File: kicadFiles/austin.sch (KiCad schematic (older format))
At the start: 469 parts, among them J1 TYPE-C-31-M12_13, J2 Conn_01x04_Male, J5 Conn_01x06_Male, Q1 AO4406AL, SW1 MXSwitch, SW10 MXSwitch, SW100 MXSwitch, SW101 MXSwitch, SW102 MXSwitch, SW103 MXSwitch, SW104 MXSwitch, SW105 MXSwitch, SW106 MXSwitch, SW107 MXSwitch, SW108 MXSwitch, SW109 MXSwitch, SW11 MXSwitch, SW110 MXSwitch, SW111 MXSwitch, SW112 MXSwitch, SW12 MXSwitch, SW13 MXSwitch, SW14 MXSwitch, SW15 MXSwitch, SW16 MXSwitch, SW17 MXSwitch, SW18 MXSwitch, SW19 MXSwitch, SW2 MXSwitch, SW20 MXSwitch, SW21 MXSwitch, SW22 MXSwitch, SW23 MXSwitch, SW24 MXSwitch, SW25 MXSwitch, SW26 MXSwitch, SW27 MXSwitch, SW28 MXSwitch, SW29 MXSwitch, SW3 MXSwitch, SW30 MXSwitch, SW31 MXSwitch, SW32 MXSwitch, SW33 MXSwitch, SW34 MXSwitch, SW35 MXSwitch, SW36 MXSwitch, SW37 MXSwitch, SW38 MXSwitch, SW39 MXSwitch, SW4 MXSwitch, SW40 MXSwitch, SW41 MXSwitch, SW42 MXSwitch, SW43 MXSwitch, SW44 MXSwitch, SW45 MXSwitch, SW46 MXSwitch, SW47 MXSwitch, SW48 MXSwitch, SW49 MXSwitch, SW5 MXSwitch, SW50 MXSwitch, SW51 MXSwitch, SW52 MXSwitch, SW53 MXSwitch, SW54 MXSwitch, SW55 MXSwitch, SW56 MXSwitch, SW57 MXSwitch, SW59 MXSwitch, SW6 MXSwitch, SW60 MXSwitch, SW61 MXSwitch, SW62 MXSwitch, SW63 MXSwitch, SW64 MXSwitch, SW65 MXSwitch, SW66 MXSwitch, SW67 MXSwitch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

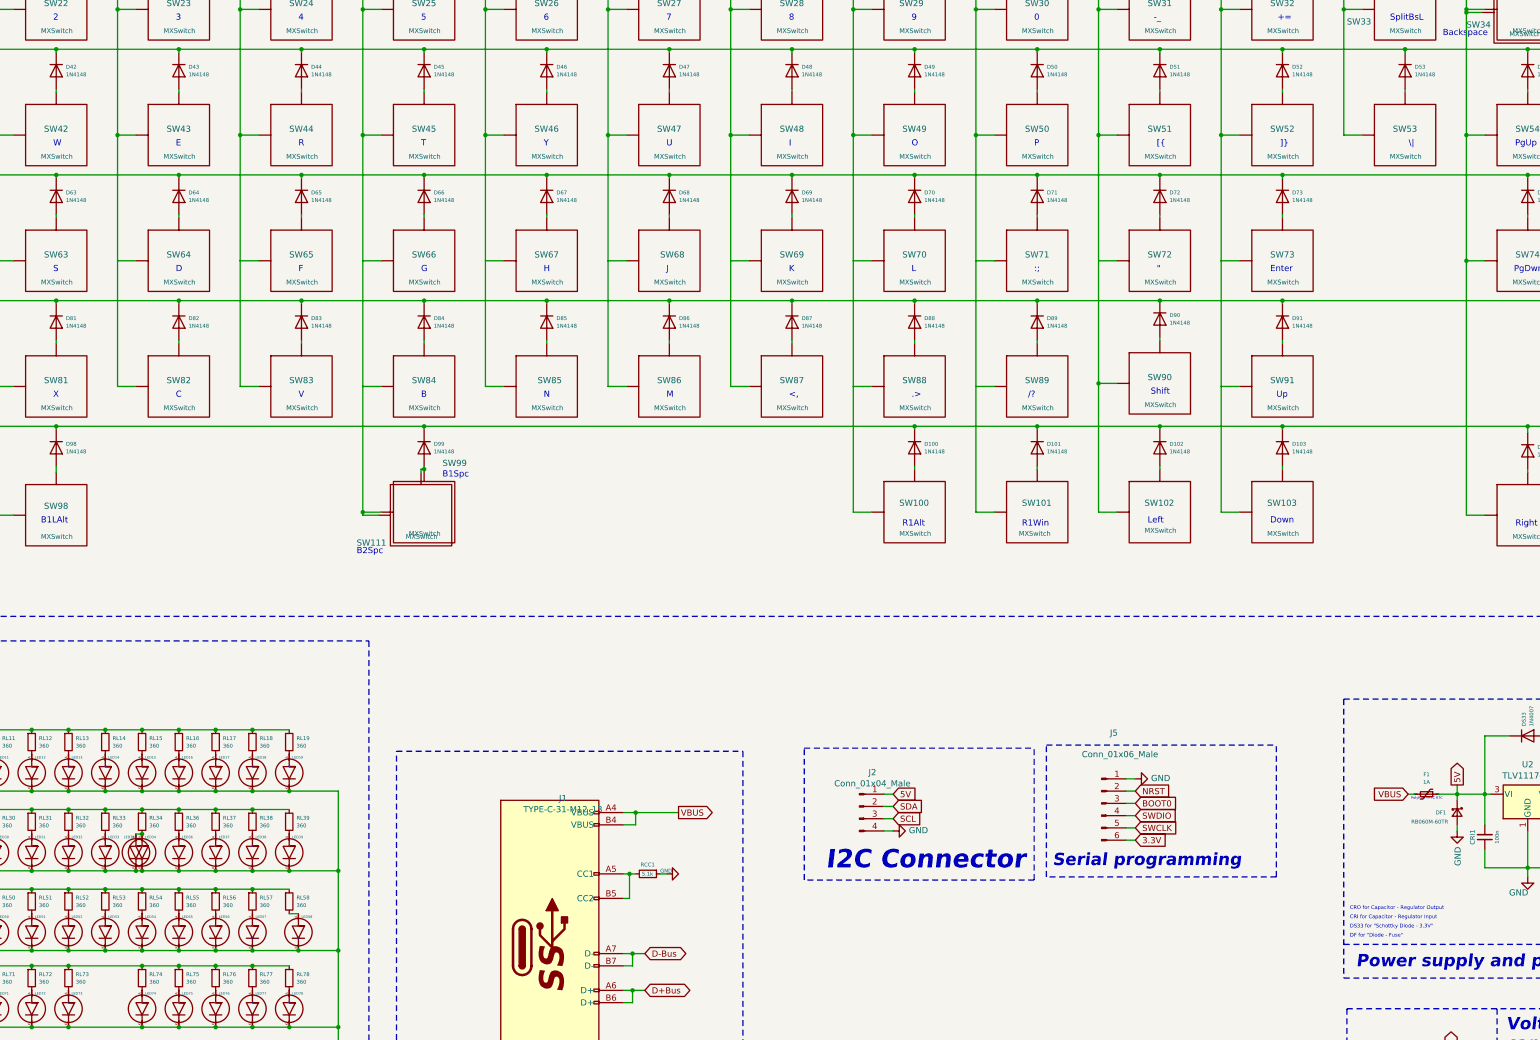
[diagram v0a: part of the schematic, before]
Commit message: [Feature] Added ISO enter
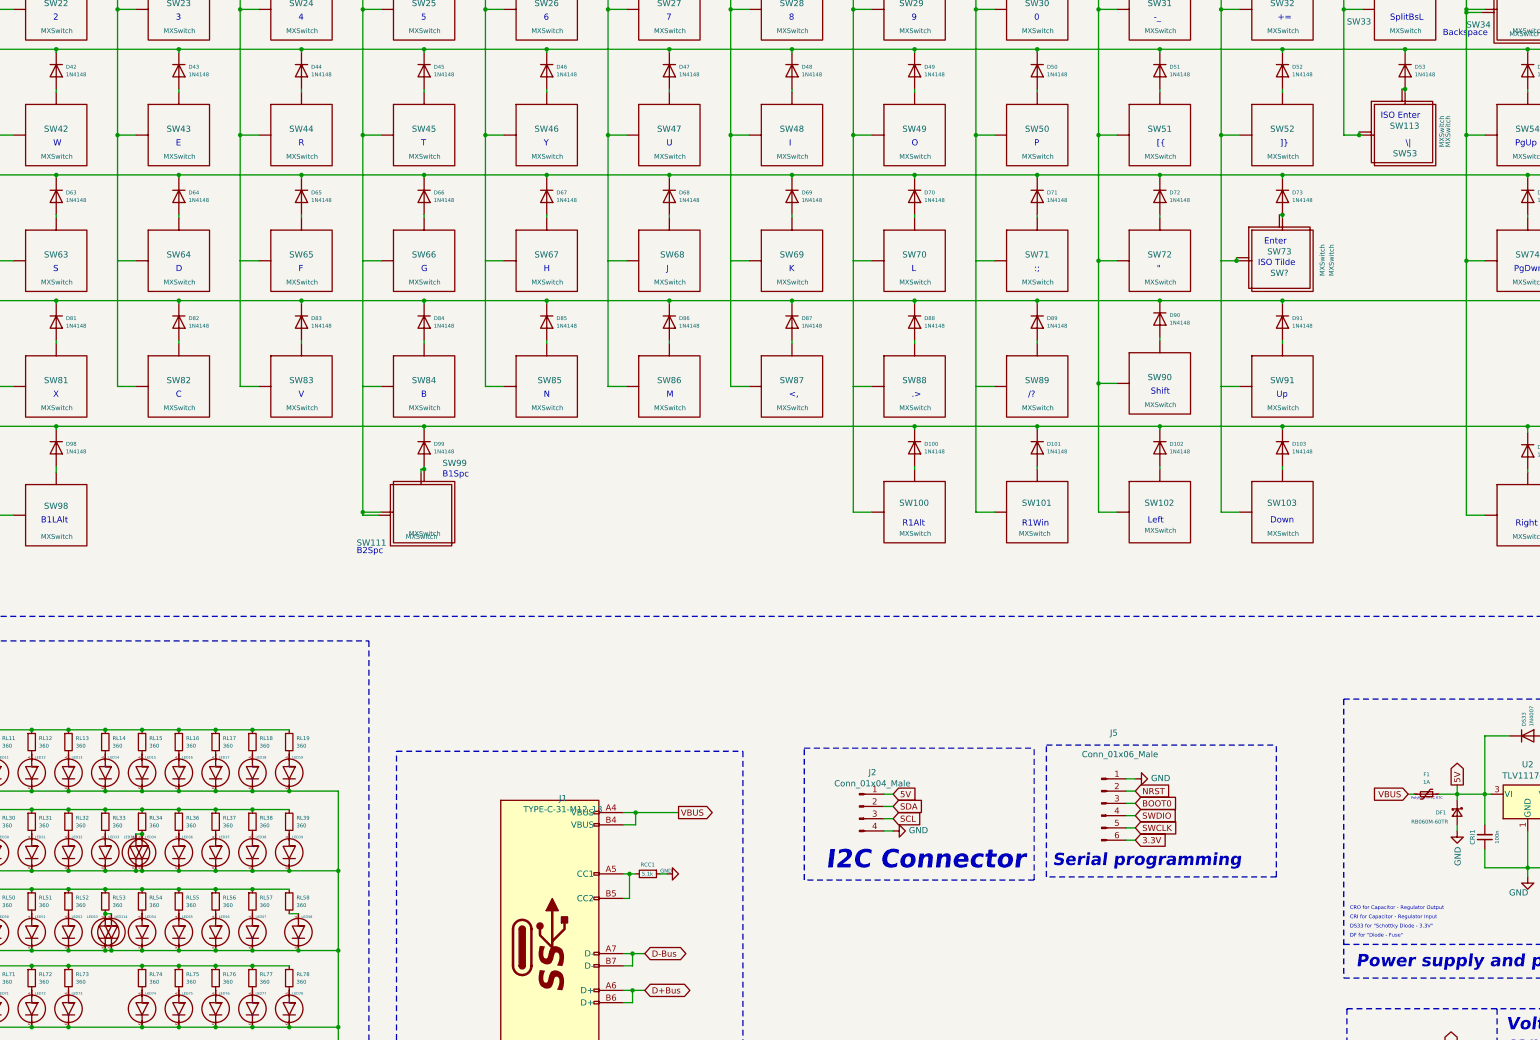
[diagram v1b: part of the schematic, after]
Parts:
- added LED114: LED, acheronComponents:LED_THT_2.54mm, symbol acheronSymbols:LED
- added SW113: MXSwitch, acheron_MX:MX_ISOEnter, symbol acheronSymbols:MXSwitch
- added SW?: MXSwitch, acheron_MX:MX225, symbol acheronSymbols:MXSwitch
- DS33: footprint Diode_SMD:D_SOD-123F -> acheronComponents:D_SOD-123
- J2: footprint acheronConnectors:4pinHeader -> acheronConnectors:HEADER_4PIN
- J5: footprint acheronConnectors:6pinHeader -> acheronConnectors:HEADER_6PIN_HORIZONTAL
- LED1, LED10, LED100, LED101, LED102, LED103, LED104, LED105, LED106, LED107, LED108, LED109, LED11, LED110, LED111, LED112, LED113, LED12, LED13, LED14, LED15, LED16, LED17, LED18, LED19, LED2, LED20, LED21, LED22, LED23, LED24, LED25, LED26, LED27, LED28, LED29, LED3, LED30, LED31, LED32, LED33, LED34, LED35, LED36, LED37, LED38, LED39, LED4, LED40, LED41, LED42, LED43, LED44, LED45, LED46, LED47, LED48, LED49, LED5, LED50, LED51, LED52, LED53, LED54, LED55, LED56, LED57, LED58, LED6, LED60, LED61, LED62, LED63, LED64, LED65, LED66, LED67, LED68, LED69, LED7, LED70, LED71, LED72, LED73, LED74, LED75, LED76, LED77, LED78, LED79, LED8, LED80, LED81, LED82, LED83, LED84, LED85, LED86, LED87, LED88, LED89, LED9, LED90, LED91, LED92, LED93, LED94, LED95, LED97, LED98, LED99, LEDCAPS1, LEDNUM1, LEDSCRL1: footprint acheronComponents:thtLED -> acheronComponents:LED_THT_2.54mm
- Q1: footprint acheronComponents:AO4406AL -> acheronComponents:SOIC-8
- R5, RCC1, RL72: footprint Resistor_SMD:R_1206_3216Metric_Pad1.42x1.75mm_HandSolder -> acheronComponents:R_SMD_1026
- RGP1, RGS1, RI1, RI2, RI3, RL1, RL10, RL100, RL101, RL102, RL103, RL104, RL105, RL106, RL107, RL108, RL11, RL12, RL13, RL14, RL15, RL16, RL17, RL18, RL19, RL2, RL20, RL21, RL22, RL23, RL24, RL25, RL26, RL27, RL28, RL29, RL3, RL30, RL31, RL32, RL33, RL34, RL36, RL37, RL38, RL39, RL4, RL40, RL41, RL42, RL43, RL44, RL45, RL46, RL47, RL48, RL49, RL5, RL50, RL51, RL52, RL53, RL54, RL55, RL56, RL57, RL58, RL6, RL60, RL62, RL63, RL64, RL65, RL66, RL67, RL68, RL69, RL7, RL70, RL71, RL73, RL74, RL75, RL76, RL77, RL78, RL79, RL8, RL80, RL81, RL82, RL83, RL84, RL85, RL86, RL87, RL88, RL89, RL9, RL90, RL91, RL92, RL93, RL94, RL95, RL96, RL97, RL98, RL99, RRST1: footprint acheronComponents:R_1026 -> acheronComponents:R_SMD_1026
- SW1, SW10, SW102, SW103, SW104, SW105, SW106, SW107, SW108, SW11, SW12, SW13, SW14, SW15, SW16, SW17, SW18, SW19, SW2, SW20, SW21, SW22, SW23, SW24, SW25, SW26, SW27, SW28, SW29, SW3, SW30, SW31, SW32, SW33, SW35, SW36, SW37, SW38, SW39, SW4, SW41, SW42, SW43, SW44, SW45, SW46, SW47, SW48, SW49, SW5, SW50, SW51, SW52, SW54, SW55, SW56, SW57, SW6, SW62, SW63, SW64, SW65, SW66, SW67, SW68, SW69, SW7, SW70, SW71, SW72, SW74, SW75, SW76, SW77, SW8, SW80, SW81, SW82, SW83, SW84, SW85, SW86, SW87, SW88, SW89, SW9, SW91, SW92, SW93, SW94: footprint acheronKeyboardSwitches:MX100 -> acheron_MX:MX100
- SW100, SW101, SW109, SW40, SW53: footprint acheronKeyboardSwitches:MX150 -> acheron_MX:MX150
- SW112: footprint acheronKeyboardSwitches:MX200R -> acheron_MX:MX200R
- SW34: footprint acheronKeyboardSwitches:MX200 -> acheron_MX:MX200
- SW60, SW90: footprint acheronKeyboardSwitches:MX175 -> acheron_MX:MX175
- SW61, SW96, SW98: footprint acheronKeyboardSwitches:MX125 -> acheron_MX:MX125
- SW73, SW79: footprint acheronKeyboardSwitches:MX225 -> acheron_MX:MX225
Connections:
- net Col12: now also SW72.1 (Col)
- net Col13: now also SW?.1 (Col)
- net Col14: now also SW113.1 (Col)
- net LEDK: now also LED114.K
- net at D73.2 (A), SW73.2 (Row): now also SW?.2 (Row)
- net at D53.2 (A), SW53.2 (Row): now also SW113.2 (Row)
- net at LED53.A, RL53.2: now also LED114.A
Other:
- note added: "ISO Enter"
- note added: "ISO Tilde"

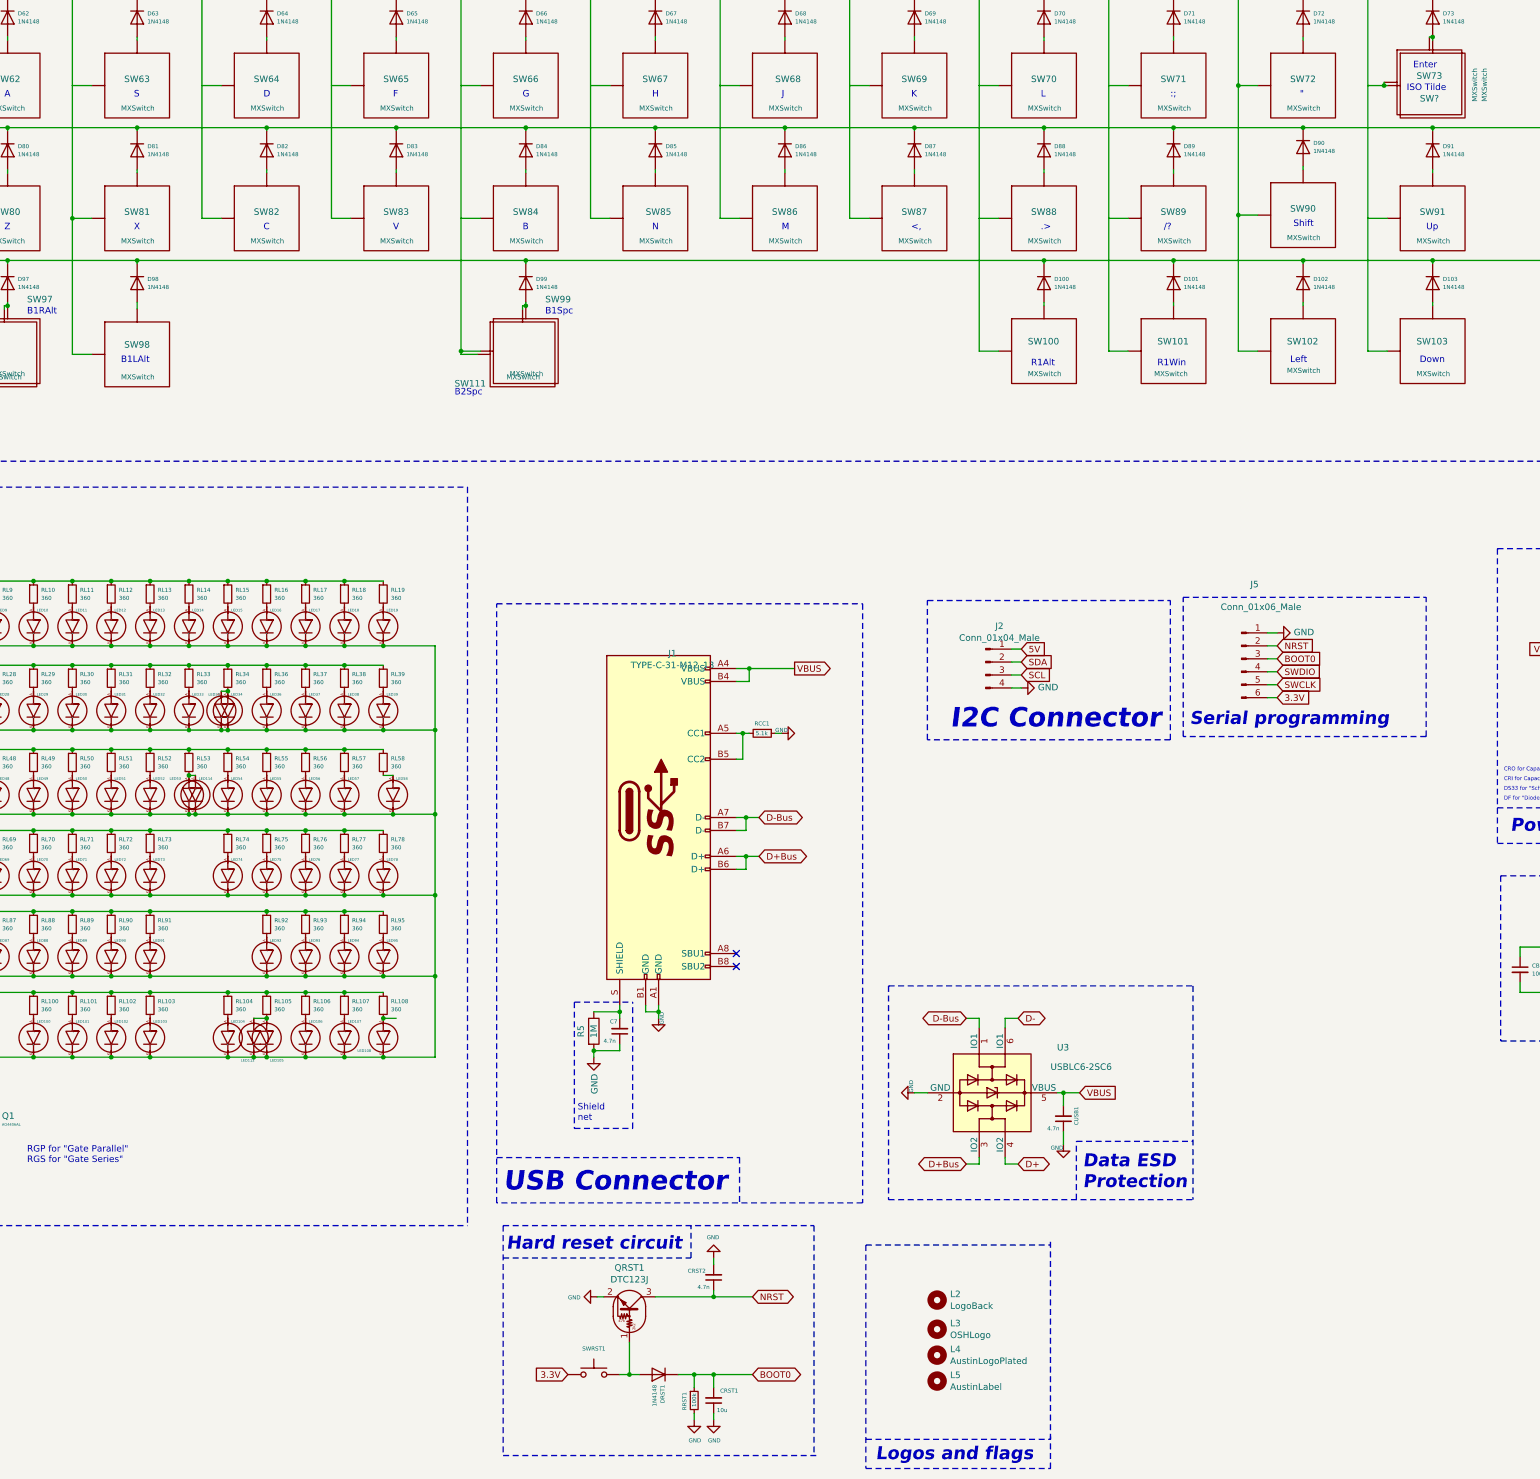
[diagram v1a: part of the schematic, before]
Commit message: [Update] Finished ISO support, added documentation.
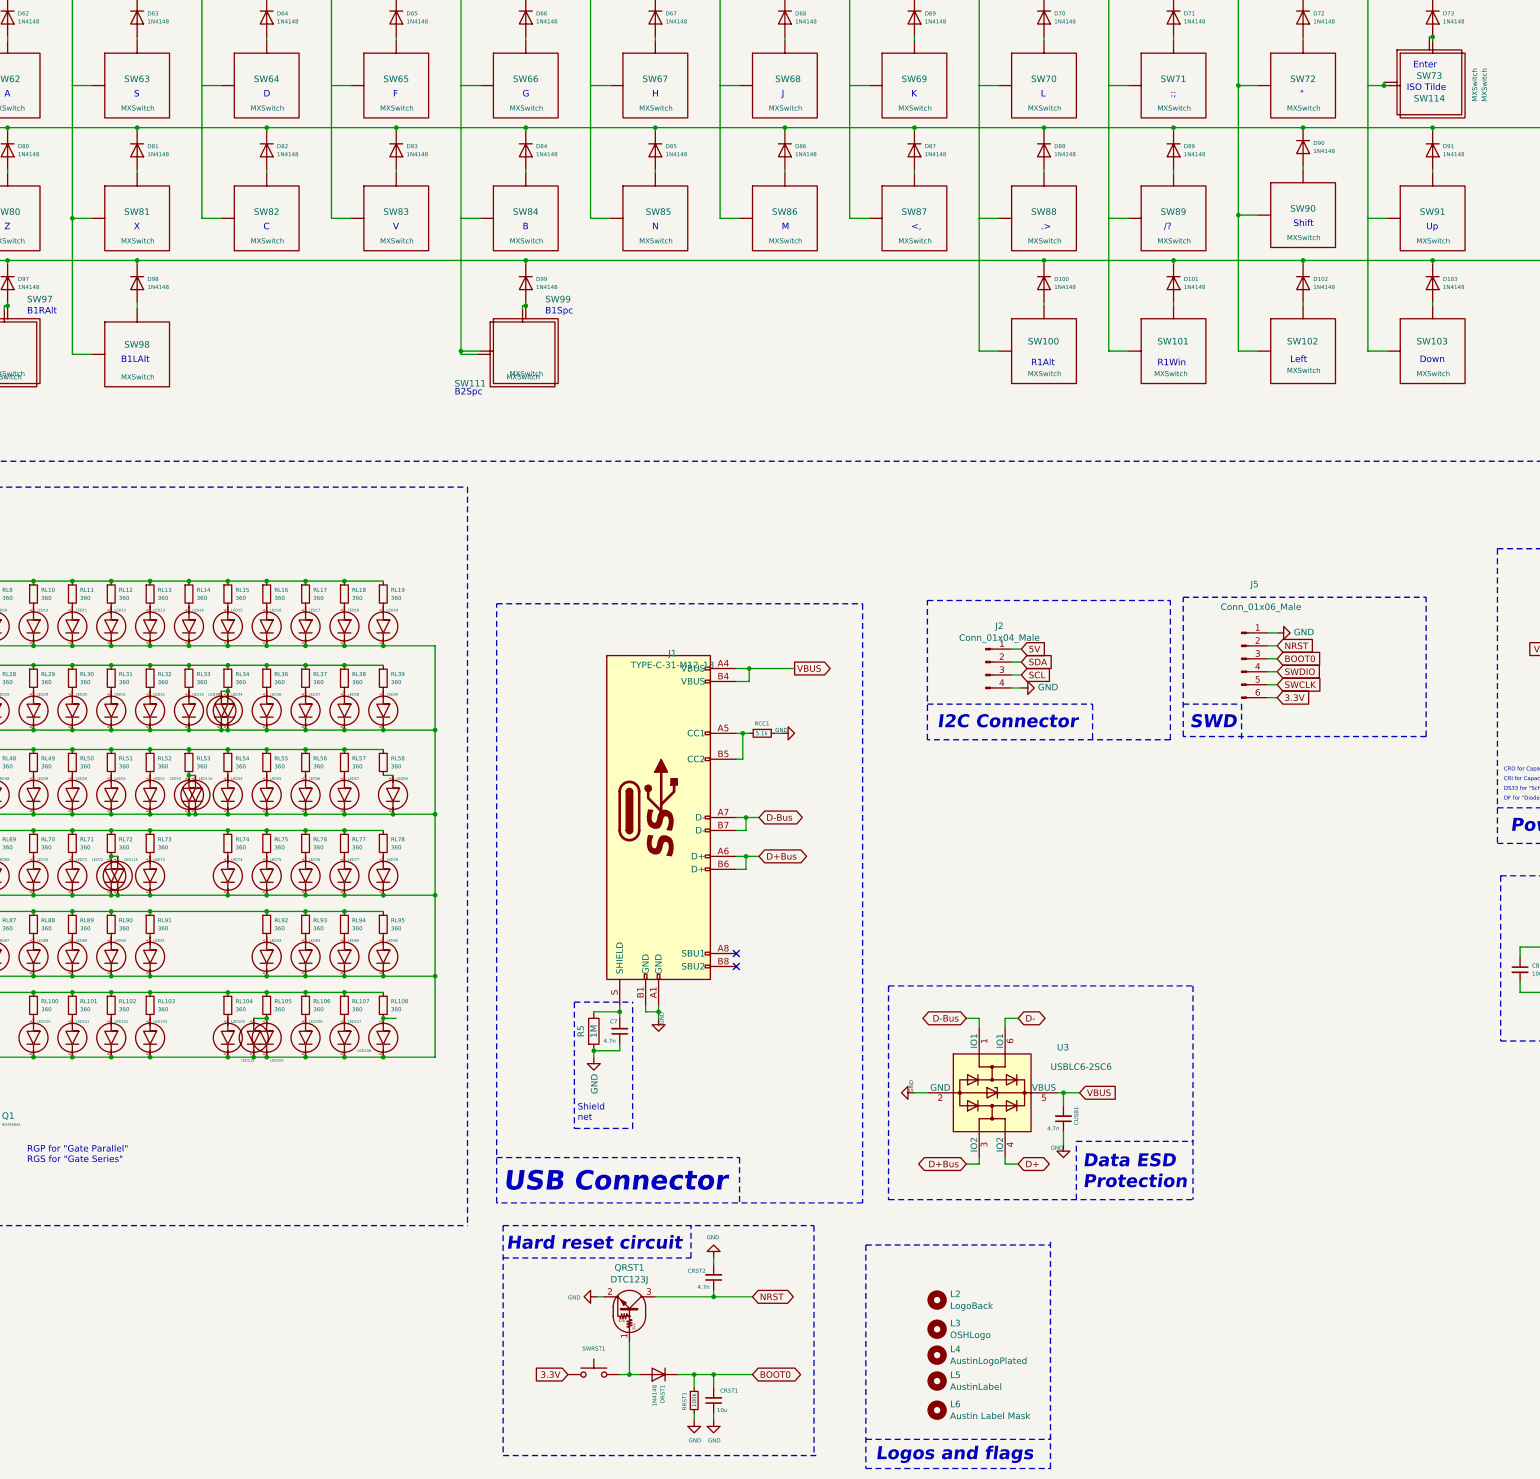
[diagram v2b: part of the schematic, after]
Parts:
- added L6: Austin Label Mask, austinLogo:austinLabelMask, symbol Mechanical:MountingHole
- added LED115: LED, acheronComponents:LED_THT_2.54mm, symbol acheronSymbols:LED
- SW114: renamed from SW?; footprint acheron_MX:MX225 -> acheron_MX:MX100
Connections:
- net LEDK: now also LED115.K
- net at LED72.A, RL72.2: now also LED115.A
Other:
- note added: "SWD"
- note removed: "Serial programming"
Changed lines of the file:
@@
 Wire Notes Line width 20
 	12575 10225 10700 10225
-Text Notes 10875 10150 0    150  Italic 30
+Text Notes 10775 10150 0    100  Italic 20
 I2C Connector
 Text GLabel 21650 11075 2    50   Input ~ 0
@@
 Wire Notes Line width 20
 	14550 10200 12675 10200
-Text Notes 12725 10125 0    100  Italic 20
-Serial programming
+Text Notes 12725 10150 0    100  Italic 20
+SWD
 Wire Notes Line width 20
 	14550 10200 14550 9125
@@
 U 1 1 5DA221B4
 P 4400 11275
-F 0 "LED72" V 4275 11300 20  0000 L CNN
+F 0 "LED72" V 4275 11125 20  0000 L CNN
 F 1 "LED" V 4250 11300 20  0001 L CNN
 F 2 "acheronComponents:LED_THT_2.54mm" H 4400 11275 50  0001 C CNN
@@
 Connection ~ 4700 11425
 Wire Wire Line
-	4400 11425 4700 11425
+	4400 11425 4450 11425
 Wire Wire Line
 	4400 10925 4700 10925
@@
 	14100 5175 14225 5175
 $Comp
-L acheronSymbols:MXSwitch SW?
+L acheronSymbols:MXSwitch SW114
 U 1 1 5E9FC89A
 P 14575 5150
-F 0 "SW?" H 14575 5025 50  0000 C CNN
+F 0 "SW114" H 14575 5025 50  0000 C CNN
 F 1 "MXSwitch" V 15000 5000 39  0000 L CNN
-F 2 "acheron_MX:MX225" H 14575 5150 50  0001 C CNN
+F 2 "acheron_MX:MX100" H 14575 5150 50  0001 C CNN
 F 3 "" H 14575 5150 50  0001 C CNN
 	1    14575 5150
@@
 Text Notes 14400 5225 0    50   ~ 0
 ISO Tilde
+$Comp
+L acheronSymbols:LED LED115
+U 1 1 5EC374A6
+P 4450 11275
+F 0 "LED115" V 4325 11325 20  0000 L CNN
+F 1 "LED" V 4300 11300 20  0001 L CNN
+F 2 "acheronComponents:LED_THT_2.54mm" H 4450 11275 50  0001 C CNN
+F 3 "" H 4450 11275 50  0001 C CNN
+	1    4450 11275
+	0    1    1    0
+$EndComp
+Connection ~ 4450 11425
+Wire Wire Line
+	4450 11425 4700 11425
+Wire Wire Line
+	4450 11125 4400 11125
+Connection ~ 4400 11125
+$Comp
+L Mechanical:MountingHole L6
+U 1 1 5EDE1DF1
+P 10775 15400
+F 0 "L6" H 10875 15446 50  0000 L CNN
+F 1 "Austin Label Mask" H 10875 15355 50  0000 L CNN
+F 2 "austinLogo:austinLabelMask" H 10775 15400 50  0001 C CNN
+F 3 "~" H 10775 15400 50  0001 C CNN
+	1    10775 15400
+	1    0    0    -1
+$EndComp
+Wire Notes Line width 20
+	10700 9950 11975 9950
+Wire Notes Line width 20
+	11975 9950 11975 10225
+Wire Notes Line width 20
+	12675 9950 13125 9950
+Wire Notes Line width 20
+	13125 9950 13125 10225
 $EndSCHEMATC

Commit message: [Feature] Added Drift Mechanics plated logo
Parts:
- added L1: Drift Mechanics Logo, austinLogo:driftMechanics_logo, symbol Mechanical:MountingHole
- U1: symbol acheronSymbols:STM32F072_LQFP48 -> austin-rescue:STM32F072_LQFP48-acheronSymbols
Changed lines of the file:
@@
 	625  8275 7150 8275
 $Comp
-L acheronSymbols:STM32F072_LQFP48 U1
+L austin-rescue:STM32F072_LQFP48-acheronSymbols U1
 U 1 1 6623D717
 P 20525 11725
@@
 Wire Notes Line width 20
 	13125 9950 13125 10225
+$Comp
+L Mechanical:MountingHole L1
+U 1 1 5D596B36
+P 10775 14350
+F 0 "L1" H 10875 14396 50  0000 L CNN
+F 1 "Drift Mechanics Logo" H 10875 14305 50  0000 L CNN
+F 2 "austinLogo:driftMechanics_logo" H 10775 14350 50  0001 C CNN
+F 3 "~" H 10775 14350 50  0001 C CNN
+	1    10775 14350
+	1    0    0    -1
+$EndComp
 $EndSCHEMATC
